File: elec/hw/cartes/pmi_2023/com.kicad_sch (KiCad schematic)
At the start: 31 parts, among them J7 USB4105-GF-A-060, Q2 2N7002, SW7 MSS12C02LS-BB2.0, U32 ESP32-S3-WROOM-1

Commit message: wip
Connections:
- net esp32_dbg_tx_3v3: now also J6.5 (RXD); no longer J6.4 (TXD)
- net gyro_irq_3v3: now reaches U32.22 (IO14,RTC_GPIO14,GPIO14,TOUCH14,FSPIWP,FSPIDQS,SUBSPIWP)
- net emergency_stop_3v3: now reaches U32.23 (IO21,RTC_GPIO21,GPIO21)
- net start_robot_3v3: now reaches U32.28 (IO35,SPIIO6,GPIO35,FSPID,SUBSPID)
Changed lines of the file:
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@@
+    (stroke (width 0) (type default))
+  )
+  (wire (pts (xy 119.38 101.6) (xy 134.62 101.6))
     (stroke (width 0) (type default))
   )
@@
   )
   (wire (pts (xy 85.09 59.69) (xy 85.09 57.15))
+    (stroke (width 0) (type default))
+  )
+  (wire (pts (xy 119.38 104.14) (xy 134.62 104.14))
     (stroke (width 0) (type default))
   )
@@
     (stroke (width 0) (type default))
   )
+  (wire (pts (xy 119.38 88.9) (xy 134.62 88.9))
+    (stroke (width 0) (type default))
+  )
   (wire (pts (xy 111.76 196.85) (xy 111.76 158.75))
     (stroke (width 0) (type dash))
@@
     (effects (font (size 1.27 1.27)) (justify right))
   )
+  (hierarchical_label "emergency_stop_3v3" (shape input) (at 119.38 101.6 180) (fields_autoplaced)
+    (effects (font (size 1.27 1.27)) (justify right))
+  )
   (hierarchical_label "scl_3v3" (shape output) (at 62.23 109.22 180) (fields_autoplaced)
     (effects (font (size 1.27 1.27)) (justify right))
@@
     (effects (font (size 1.27 1.27)) (justify right))
   )
+  (hierarchical_label "gyro_irq_3v3" (shape input) (at 119.38 88.9 180) (fields_autoplaced)
+    (effects (font (size 1.27 1.27)) (justify right))
+  )
   (hierarchical_label "i_prop_left_3v3" (shape input) (at 123.19 58.42 180) (fields_autoplaced)
     (effects (font (size 1.27 1.27)) (justify right))
@@
   )
   (hierarchical_label "right_encod_A_3v3" (shape input) (at 119.38 116.84 180) (fields_autoplaced)
+    (effects (font (size 1.27 1.27)) (justify right))
+  )
+  (hierarchical_label "start_robot_3v3" (shape input) (at 119.38 104.14 180) (fields_autoplaced)
     (effects (font (size 1.27 1.27)) (justify right))
   )
@@
     (pin "3")
     (pin "4")
-    (pin "4")
+    (pin "5")
     (pin "6")
     (instances

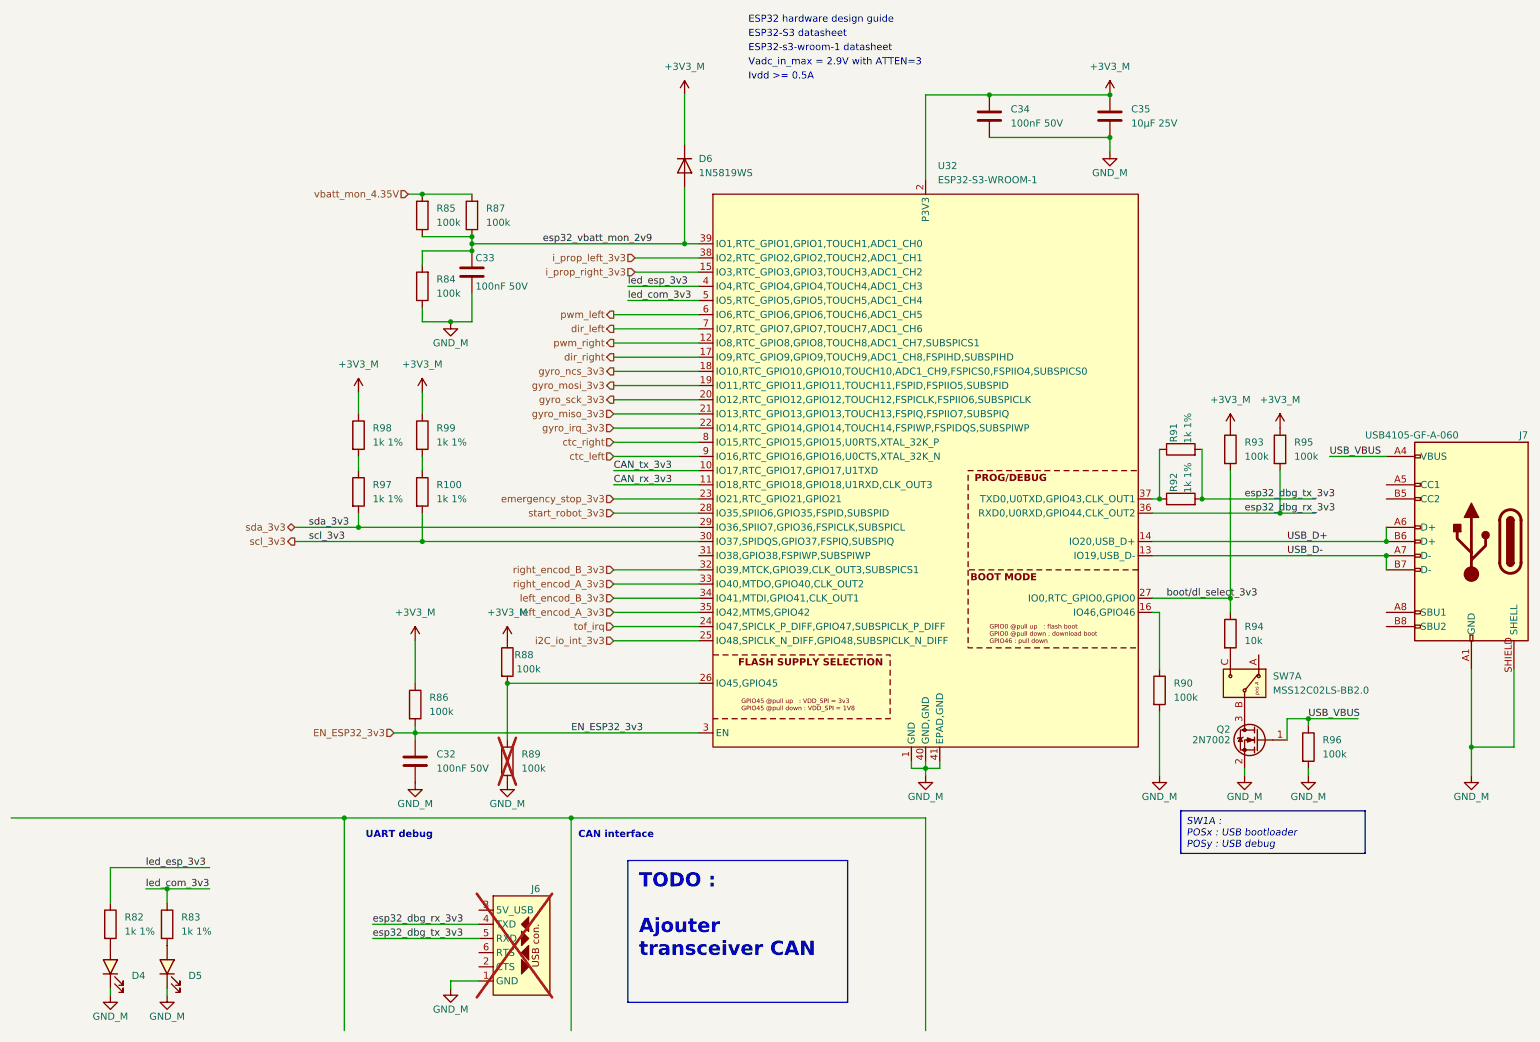
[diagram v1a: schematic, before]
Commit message: front and back tof added, selector changed, ready to route
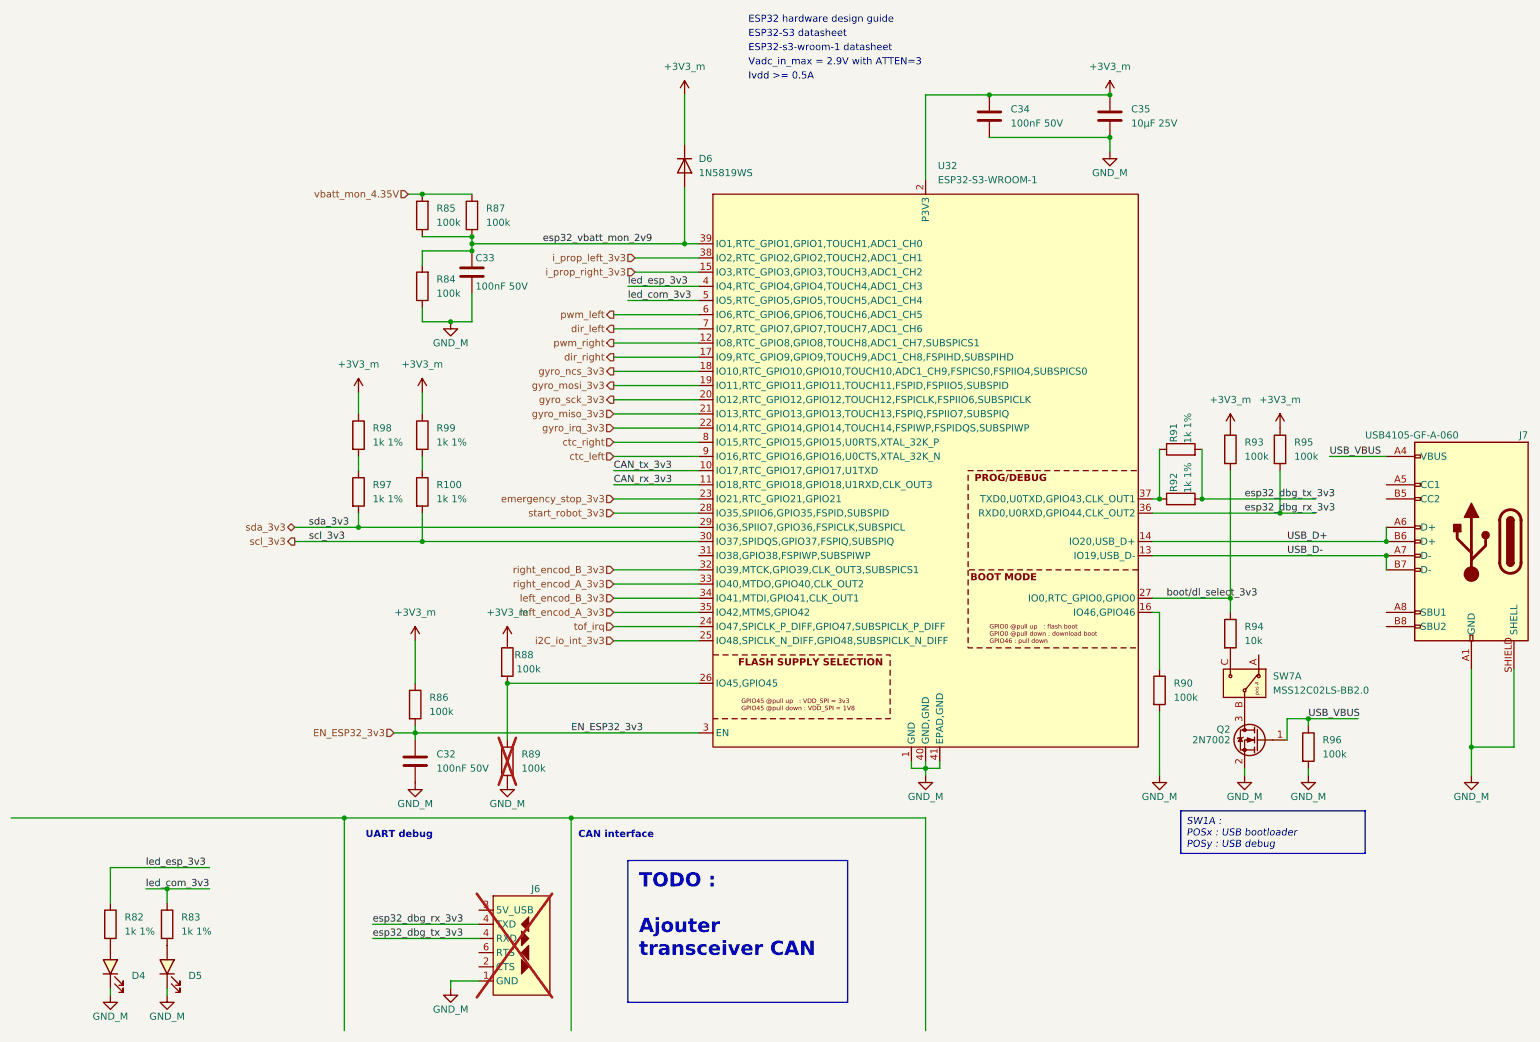
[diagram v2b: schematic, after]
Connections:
- net esp32_dbg_tx_3v3: now also J6.4 (TXD); no longer J6.5 (RXD)

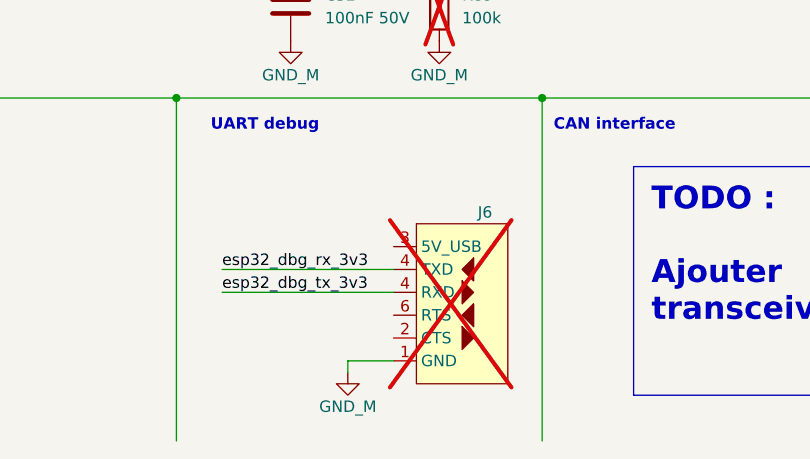
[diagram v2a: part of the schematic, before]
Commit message: corrected librariesand ongoing routing
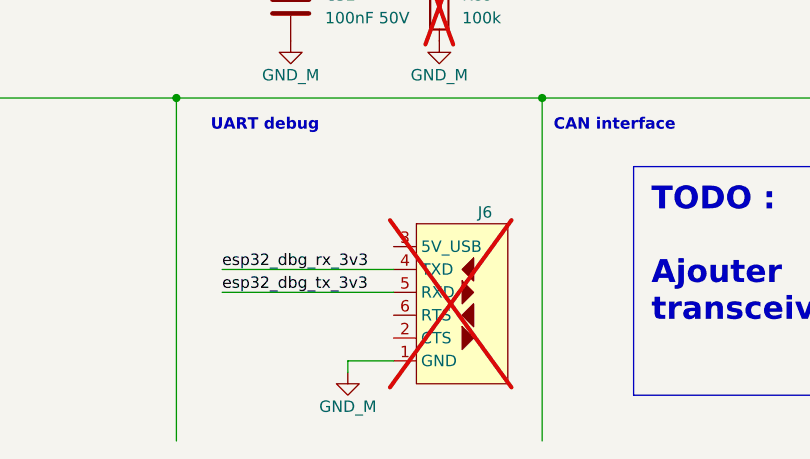
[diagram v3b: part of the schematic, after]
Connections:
- net esp32_dbg_tx_3v3: now also J6.5 (RXD); no longer J6.4 (TXD)
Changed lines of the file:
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@@
 		(pin "4"
 		)
-		(pin "4"
+		(pin "5"
 		)
 		(pin "6"

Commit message: wip
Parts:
- R100, R82, R83, R91, R92, R97, R98, R99: Specification 1k 0603 1% 100mW -> 10k 0603 1% 100mW; mouser (none) -> 603-RC0603FR-10100KL
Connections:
- net CAN_rx_3v3: no longer U32.11 (IO18,RTC_GPIO18,GPIO18,U1RXD,CLK_OUT3)
- net CAN_tx_3v3: no longer U32.10 (IO17,RTC_GPIO17,GPIO17,U1TXD)
- net ctc_left: now also U32.6 (IO6,RTC_GPIO6,GPIO6,TOUCH6,ADC1_CH5); no longer U32.9 (IO16,RTC_GPIO16,GPIO16,U0CTS,XTAL_32K_N)
- net ctc_right: now also U32.24 (IO47,SPICLK_P_DIFF,GPIO47,SUBSPICLK_P_DIFF); no longer U32.8 (IO15,RTC_GPIO15,GPIO15,U0RTS,XTAL_32K_P)
- net dir_left: now also U32.22 (IO14,RTC_GPIO14,GPIO14,TOUCH14,FSPIWP,FSPIDQS,SUBSPIWP); no longer U32.7 (IO7,RTC_GPIO7,GPIO7,TOUCH7,ADC1_CH6)
- net dir_right: now also U32.20 (IO12,RTC_GPIO12,GPIO12,TOUCH12,FSPICLK,FSPIIO6,SUBSPICLK); no longer U32.17 (IO9,RTC_GPIO9,GPIO9,TOUCH9,ADC1_CH8,FSPIHD,SUBSPIHD)
- net emergency_stop_3v3: now also U32.8 (IO15,RTC_GPIO15,GPIO15,U0RTS,XTAL_32K_P); no longer U32.23 (IO21,RTC_GPIO21,GPIO21)
- net gyro_irq_3v3: now also U32.31 (IO38,GPIO38,FSPIWP,SUBSPIWP); no longer U32.22 (IO14,RTC_GPIO14,GPIO14,TOUCH14,FSPIWP,FSPIDQS,SUBSPIWP)
- net gyro_miso_3v3: now also U32.28 (IO35,SPIIO6,GPIO35,FSPID,SUBSPID); no longer U32.21 (IO13,RTC_GPIO13,GPIO13,TOUCH13,FSPIQ,FSPIIO7,SUBSPIQ)
- net gyro_mosi_3v3: now also U32.29 (IO36,SPIIO7,GPIO36,FSPICLK,SUBSPICL); no longer U32.19 (IO11,RTC_GPIO11,GPIO11,TOUCH11,FSPID,FSPIIO5,SUBSPID)
- net gyro_ncs_3v3: now also U32.30 (IO37,SPIDQS,GPIO37,FSPIQ,SUBSPIQ); no longer U32.18 (IO10,RTC_GPIO10,GPIO10,TOUCH10,ADC1_CH9,FSPICS0,FSPIIO4,SUBSPICS0)
- net gyro_sck_3v3: now also U32.25 (IO48,SPICLK_N_DIFF,GPIO48,SUBSPICLK_N_DIFF); no longer U32.20 (IO12,RTC_GPIO12,GPIO12,TOUCH12,FSPICLK,FSPIIO6,SUBSPICLK)
- net i2C_io_int_3v3: now also U32.19 (IO11,RTC_GPIO11,GPIO11,TOUCH11,FSPID,FSPIIO5,SUBSPID); no longer U32.25 (IO48,SPICLK_N_DIFF,GPIO48,SUBSPICLK_N_DIFF)
- net i_prop_left_3v3: now also U32.18 (IO10,RTC_GPIO10,GPIO10,TOUCH10,ADC1_CH9,FSPICS0,FSPIIO4,SUBSPICS0); no longer U32.38 (IO2,RTC_GPIO2,GPIO2,TOUCH2,ADC1_CH1)
- net i_prop_right_3v3: now also U32.17 (IO9,RTC_GPIO9,GPIO9,TOUCH9,ADC1_CH8,FSPIHD,SUBSPIHD); no longer U32.15 (IO3,RTC_GPIO3,GPIO3,TOUCH3,ADC1_CH2)
- net left_encod_A_3v3: now also U32.32 (IO39,MTCK,GPIO39,CLK_OUT3,SUBSPICS1); no longer U32.35 (IO42,MTMS,GPIO42)
- net left_encod_B_3v3: now also U32.33 (IO40,MTDO,GPIO40,CLK_OUT2); no longer U32.34 (IO41,MTDI,GPIO41,CLK_OUT1)
- net pwm_left: now also U32.23 (IO21,RTC_GPIO21,GPIO21); no longer U32.6 (IO6,RTC_GPIO6,GPIO6,TOUCH6,ADC1_CH5)
- net pwm_right: now also U32.21 (IO13,RTC_GPIO13,GPIO13,TOUCH13,FSPIQ,FSPIIO7,SUBSPIQ); no longer U32.12 (IO8,RTC_GPIO8,GPIO8,TOUCH8,ADC1_CH7,SUBSPICS1)
- net right_encod_A_3v3: now also U32.35 (IO42,MTMS,GPIO42); no longer U32.33 (IO40,MTDO,GPIO40,CLK_OUT2)
- net right_encod_B_3v3: now also U32.34 (IO41,MTDI,GPIO41,CLK_OUT1); no longer U32.32 (IO39,MTCK,GPIO39,CLK_OUT3,SUBSPICS1)
- net scl_3v3: now also R97.2, U32.10 (IO17,RTC_GPIO17,GPIO17,U1TXD); no longer R100.2, U32.30 (IO37,SPIDQS,GPIO37,FSPIQ,SUBSPIQ)
- net sda_3v3: now also R100.2, U32.11 (IO18,RTC_GPIO18,GPIO18,U1RXD,CLK_OUT3); no longer R97.2, U32.29 (IO36,SPIIO7,GPIO36,FSPICLK,SUBSPICL)
- net start_robot_3v3: now also U32.38 (IO2,RTC_GPIO2,GPIO2,TOUCH2,ADC1_CH1); no longer U32.28 (IO35,SPIIO6,GPIO35,FSPID,SUBSPID)
- net tof_irq: now also U32.12 (IO8,RTC_GPIO8,GPIO8,TOUCH8,ADC1_CH7,SUBSPICS1); no longer U32.24 (IO47,SPICLK_P_DIFF,GPIO47,SUBSPICLK_P_DIFF)
- new net conf3_3v3: U32.7 (IO7,RTC_GPIO7,GPIO7,TOUCH7,ADC1_CH6)
- new net enable_tof_3v3: U32.9 (IO16,RTC_GPIO16,GPIO16,U0CTS,XTAL_32K_N)
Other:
- note added: "GPIO3 : pull up au demarrage"
- moved on the sheet: R100, R86, R97, R98, R99
